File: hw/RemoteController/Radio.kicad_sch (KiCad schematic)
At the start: 49 parts, among them J4 BWSMA-KE-Z001, U10 H3-TCD-12-222X+, U5 XA17-G4K, U8 AD8313xRM, U9 GVA-63, Y2 6.6128 MHz, Y3 10.7 MHz, Y4 13.56 MHz

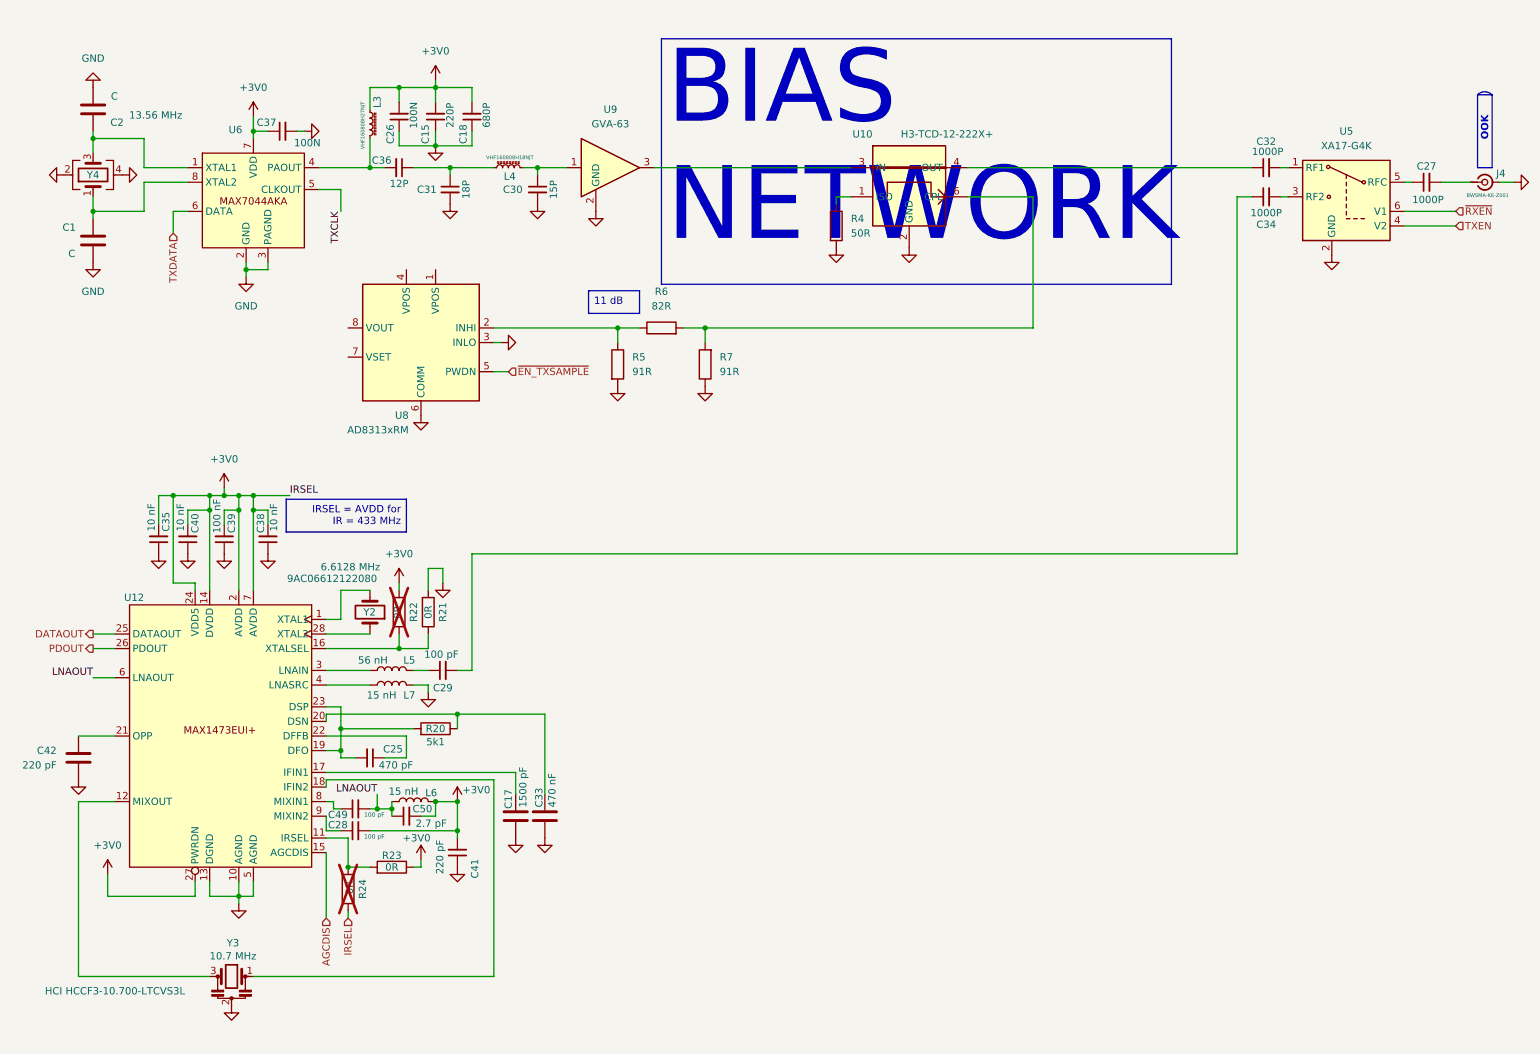
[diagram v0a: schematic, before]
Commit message: remote_ctrl: finish schematic
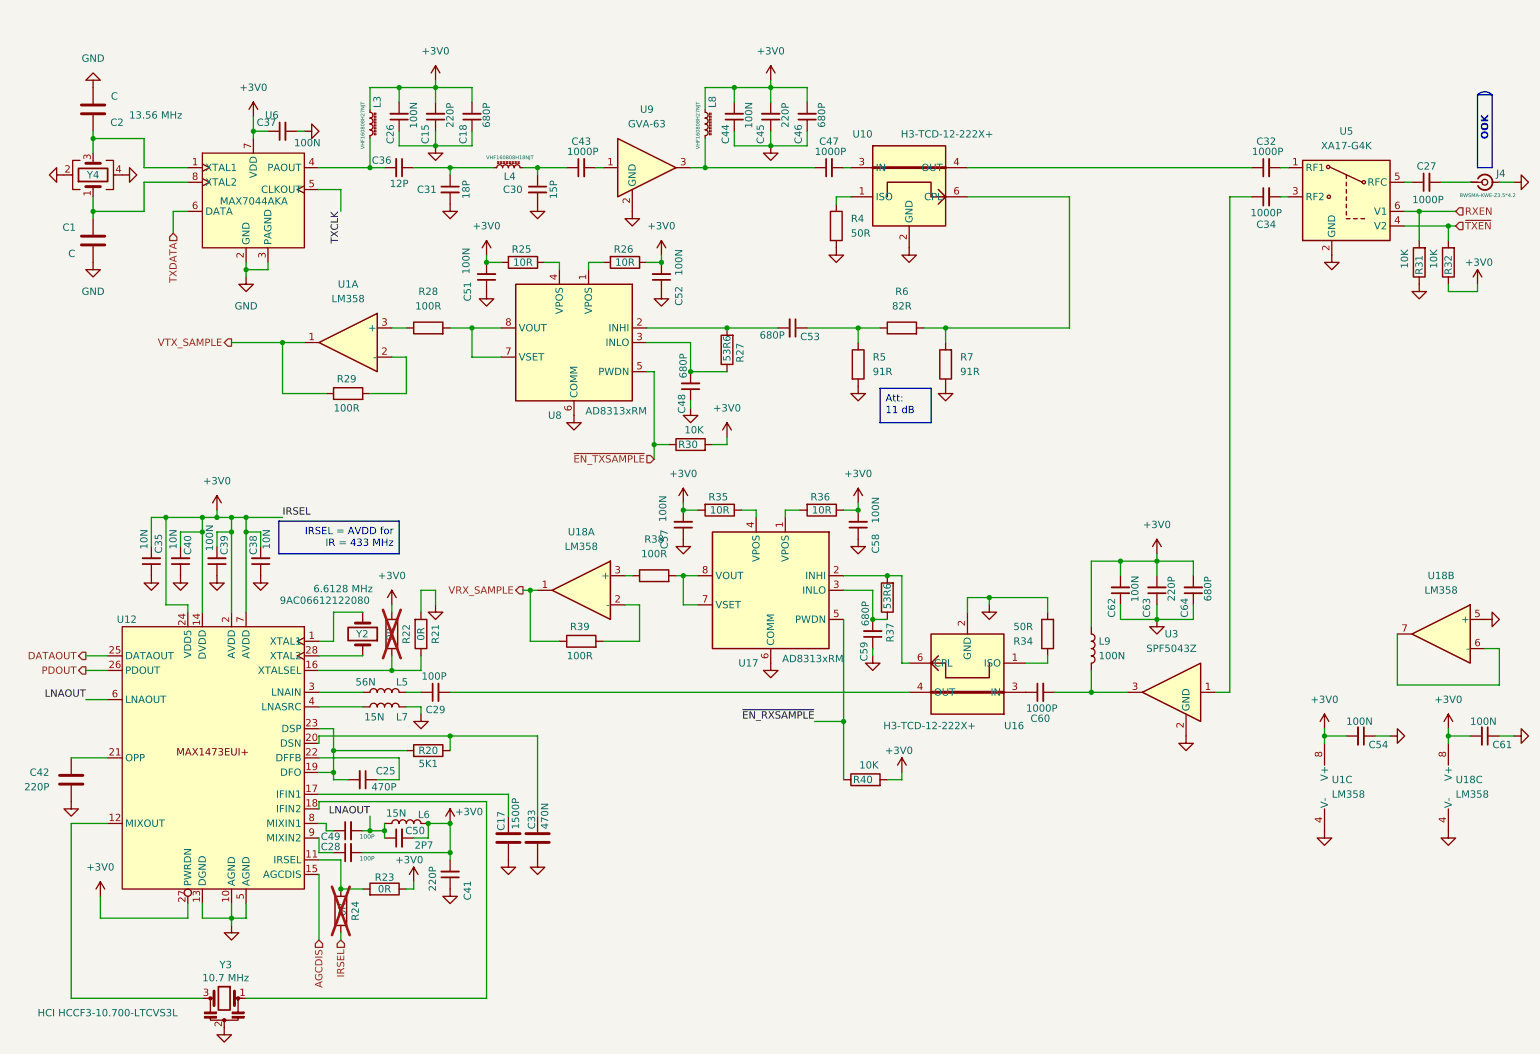
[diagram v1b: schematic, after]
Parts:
- added C43, C47, C60: 1000P, Capacitor_SMD:C_0603_1608Metric_Pad1.08x0.95mm_HandSolder, symbol Device:C_Small
- added C44, C51, C52, C54, C57, C58, C61, C62: 100N, Capacitor_SMD:C_0603_1608Metric_Pad1.08x0.95mm_HandSolder, symbol Device:C_Small
- added C45, C63: 220P, Capacitor_SMD:C_0603_1608Metric_Pad1.08x0.95mm_HandSolder, symbol Device:C_Small
- added C46, C48, C53, C59, C64: 680P, Capacitor_SMD:C_0603_1608Metric_Pad1.08x0.95mm_HandSolder, symbol Device:C_Small
- added L8: 27N, Inductor_SMD:L_0603_1608Metric_Pad1.05x0.95mm_HandSolder, symbol Device:L_Ferrite_Small
- added L9: 100N, Inductor_SMD:L_0603_1608Metric_Pad1.05x0.95mm_HandSolder, symbol Device:L
- added R25, R26, R35, R36: 10R, Resistor_SMD:R_0603_1608Metric_Pad0.98x0.95mm_HandSolder, symbol Device:R
- added R27, R37: 53R6, Resistor_SMD:R_0603_1608Metric_Pad0.98x0.95mm_HandSolder, symbol Device:R
- added R28, R29, R38, R39: 100R, Resistor_SMD:R_0603_1608Metric_Pad0.98x0.95mm_HandSolder, symbol Device:R
- added R30, R31, R32, R40: 10K, Resistor_SMD:R_0603_1608Metric_Pad0.98x0.95mm_HandSolder, symbol Device:R
- added R34: 50R, Resistor_SMD:R_0603_1608Metric_Pad0.98x0.95mm_HandSolder, symbol Device:R
- added U1, U18: LM358, Package_SO:SOIC-8_3.9x4.9mm_P1.27mm, symbol Amplifier_Operational:LM358
- added U16: H3-TCD-12-222X+, symbol steew:H3-TCD-12-222X+
- added U17: AD8313xRM, Package_SO:MSOP-8_3x3mm_P0.65mm, symbol RF_Amplifier:AD8313xRM
- added U3: SPF5043Z, Package_TO_SOT_SMD:SOT-343_SC-70-4, symbol steew:SPF5043Z
- C17: value 1500 pF -> 1500P
- C25: value 470 pF -> 470P
- C28, C29, C49: value 100 pF -> 100P
- C33: value 470 nF -> 470N
- C35, C38, C40: value 10 nF -> 10N
- C39: value 100 nF -> 100N
- C41, C42: value 220 pF -> 220P
- C50: value 2.7 pF -> 2P7
- J4: value BWSMA-KE-Z001 -> BWSMA-KWE-Z3.5*4.2; footprint Connector_Coaxial:SMB_Jack_Vertical -> Connector_Coaxial:SMA_BAT_Wireless_BWSMA-KWE-Z001; PN BWSMA-KE-Z001 -> BWSMA-KWE-Z3.5*4.2
- L5: value 56 nH -> 56N
- L6, L7: value 15 nH -> 15N
- R20: value 5k1 -> 5K1
- U6: value (none) -> MAX7044AKA; footprint steew:MAX7044AKA -> Package_TO_SOT_SMD:TSOT-23-8_HandSoldering
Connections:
- net +3V0: now also C44.2, C45.2, C46.2, C51.2, C52.2, C54.2, C57.2, C58.2, C61.2, C62.2, C63.2, C64.2, L8.1, L9.1, R25.2, R26.1, R30.2, R32.1, R35.2, R36.1, R40.2, U1.8 (V+), U18.8 (V+)
- net GND: now also C44.1, C45.1, C46.1, C48.1, C51.1, C52.1, C54.1, C57.1, C58.1, C59.1, C61.1, C62.1, C63.1, C64.1, R31.1, R34.2, U1.4 (V-), U16.2 (GND), U17.6 (COMM), U18.4 (V-), U18.5 (+), U3.2 (GND), U3.4 (GND); no longer U8.3 (INLO)
- net ~{EN_TXSAMPLE}: now also R30.1
- net at C30.1, L4.2: now also C43.1; no longer U9.1
- net at R5.1, R6.1: now also C53.1; no longer U8.2 (INHI)
- net at U8.1 (VPOS): now also R26.2
- net at U8.4 (VPOS): now also R25.1
- net at U8.7 (VSET): now also U8.8 (VOUT), R28.2
- net at U9.3: now also C47.1, L8.2; no longer U10.3 (IN)
- net at C34.1: now also U3.1; no longer C29.2
- net TXEN renamed ~{TXEN}
- net ~{TXEN}: now also R32.2
- net ~{RXEN} renamed RXEN
- net RXEN: now also R31.2
- new net: C60.2, L9.2, U3.3
- new net: R36.2, U17.1 (VPOS)
- new net: R37.2, U16.6 (CPL), U17.2 (INHI)
- new net: C59.2, R37.1, U17.3 (INLO)
- new net: R35.1, U17.4 (VPOS)
- new net: R38.2, U17.7 (VSET), U17.8 (VOUT)
- new net: R34.1, U16.1 (ISO)
- new net: C47.2, U10.3 (IN)
- new net: C60.1, U16.3 (IN)
- new net: C29.2, U16.4 (OUT)
- new net: C53.2, R27.2, U8.2 (INHI)
- new net: C48.2, R27.1, U8.3 (INLO)
- new net: R28.1, U1.3 (+)
- new net: U18.6 (-), U18.7
- new net: C43.2, U9.1
- new net: R39.2, U18.2 (-)
- new net: R38.1, U18.3 (+)
- new net: R29.2, U1.2 (-)
- new net VRX_SAMPLE: R39.1, U18.1
- new net VTX_SAMPLE: R29.1, U1.1
- new net ~{EN_RXSAMPLE}: R40.1, U17.5 (PWDN)
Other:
- moved on the sheet: C17, C25, C28, C29, C33, C35, C38, C39, C40, C41, C42, C49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

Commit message: remote_ctrl: re-start PCB
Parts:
- U12: value (none) -> MAX1473EUI+; footprint steew:MAX1473EUI+ -> Package_SO:TSSOP-28_4.4x9.7mm_P0.65mm
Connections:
- net at U16.4 (OUT): now also C29.2
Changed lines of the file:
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@@
-	)
-	(symbol
-		(lib_id "steew:MAX1473EUI+")
-		(at 64.77 121.92 0)
-		(mirror y)
-		(unit 1)
-		(body_style 1)
-		(exclude_from_sim no)
-		(in_bom yes)
-		(on_board yes)
-		(in_pos_files yes)
-		(dnp no)
-		(property "Reference" "U12"
-			(at 38.1 121.92 0)
-			(show_name no)
-			(do_not_autoplace no)
-			(effects
-				(font
-					(size 1.27 1.27)
-				)
-				(justify left)
-			)
-		)
-		(property "Value" ""
-			(at 44.8467 121.92 0)
-			(show_name no)
-			(do_not_autoplace no)
-			(effects
-				(font
-					(size 1.27 1.27)
-				)
-				(justify left)
-			)
-		)
-		(property "Footprint" "steew:MAX1473EUI+"
-			(at 64.77 121.92 0)
-			(hide yes)
-			(show_name no)
-			(do_not_autoplace no)
-			(effects
-				(font
-					(size 1.27 1.27)
-				)
-			)
-		)
-		(property "Datasheet" ""
-			(at 64.77 121.92 0)
-			(hide yes)
-			(show_name no)
-			(do_not_autoplace no)
-			(effects
-				(font
-					(size 1.27 1.27)
-				)
-			)
-		)
-		(property "Description" ""
-			(at 64.77 121.92 0)
-			(hide yes)
-			(show_name no)
-			(do_not_autoplace no)
-			(effects
-				(font
-					(size 1.27 1.27)
-				)
-			)
-		)
-		(pin "13"
-		)
-		(pin "25"
-		)
-		(pin "9"
-		)
-		(pin "15"
-		)
-		(pin "21"
-		)
-		(pin "26"
-		)
-		(pin "18"
-		)
-		(pin "19"
-		)
-		(pin "5"
-		)
-		(pin "10"
-		)
-		(pin "20"
-		)
-		(pin "14"
-		)
-		(pin "11"
-		)
-		(pin "12"
-		)
-		(pin "22"
-		)
-		(pin "23"
-		)
-		(pin "4"
-		)
-		(pin "3"
-		)
-		(pin "16"
-		)
-		(pin "28"
-		)
-		(pin "1"
-		)
-		(pin "7"
-		)
-		(pin "17"
-		)
-		(pin "24"
-		)
-		(pin "2"
-		)
-		(pin "8"
-		)
-		(pin "6"
-		)
-		(pin "27"
-		)
-		(instances
-			(project "RemoteController"
-				(path "/2496396e-da71-4b2e-9ac4-452e5130442d/d59aad70-30f5-48a2-8092-bdb11e43ed29"
-					(reference "U12")
-					(unit 1)
-				)
-			)
-		)
 	)
 	(symbol
@@
 					(unit 1)
 				)
+			)
+		)
+	)
+	(symbol
+		(lib_id "steew:MAX1473EUI+")
+		(at 52.07 123.19 0)
+		(unit 1)
+		(body_style 1)
+		(exclude_from_sim no)
+		(in_bom yes)
+		(on_board yes)
+		(in_pos_files yes)
+		(dnp no)
+		(property "Reference" "U12"
+			(at 45.466 143.002 0)
+			(show_name no)
+			(do_not_autoplace no)
+			(effects
+				(font
+					(size 1.27 1.27)
+				)
+				(justify left)
+			)
+		)
+		(property "Value" "MAX1473EUI+"
+			(at 45.466 145.034 0)
+			(show_name no)
+			(do_not_autoplace no)
+			(effects
+				(font
+					(size 1.27 1.27)
+				)
+				(justify left)
+			)
+		)
+		(property "Footprint" "Package_SO:TSSOP-28_4.4x9.7mm_P0.65mm"
+			(at 52.07 123.19 0)
+			(hide yes)
+			(show_name no)
+			(do_not_autoplace no)
+			(effects
+				(font
+					(size 1.27 1.27)
+				)
+			)
+		)
+		(property "Datasheet" "https://www.analog.com/media/en/technical-documentation/data-sheets/MAX1473.pdf"
+			(at 52.07 123.19 0)
+			(hide yes)
+			(show_name no)
+			(do_not_autoplace no)
+			(effects
+				(font
+					(size 1.27 1.27)
+				)
+			)
+		)
+		(property "Description" ""
+			(at 52.07 123.19 0)
+			(hide yes)
+			(show_name no)
+			(do_not_autoplace no)
+			(effects
+				(font
+					(size 1.27 1.27)
+				)
+			)
+		)
+		(pin "13"
+		)
+		(pin "25"
+		)
+		(pin "9"
+		)
+		(pin "15"
+		)
+		(pin "21"
+		)
+		(pin "26"
+		)
+		(pin "18"
+		)
+		(pin "19"
+		)
+		(pin "5"
+		)
+		(pin "10"
+		)
+		(pin "20"
+		)
+		(pin "14"
+		)
+		(pin "11"
+		)
+		(pin "12"
+		)
+		(pin "22"
+		)
+		(pin "23"
+		)
+		(pin "4"
+		)
+		(pin "3"
+		)
+		(pin "16"
+		)
+		(pin "28"
+		)
+		(pin "1"
+		)
+		(pin "7"
+		)
+		(pin "17"
+		)
+		(pin "24"
+		)
+		(pin "2"
+		)
+		(pin "8"
+		)
+		(pin "6"
+		)
+		(pin "27"
+		)
+		(instances
+			(project "RemoteController"
+				(path "/2496396e-da71-4b2e-9ac4-452e5130442d/d59aad70-30f5-48a2-8092-bdb11e43ed29"
+					(reference "U12")
+					(unit 1)
+				)

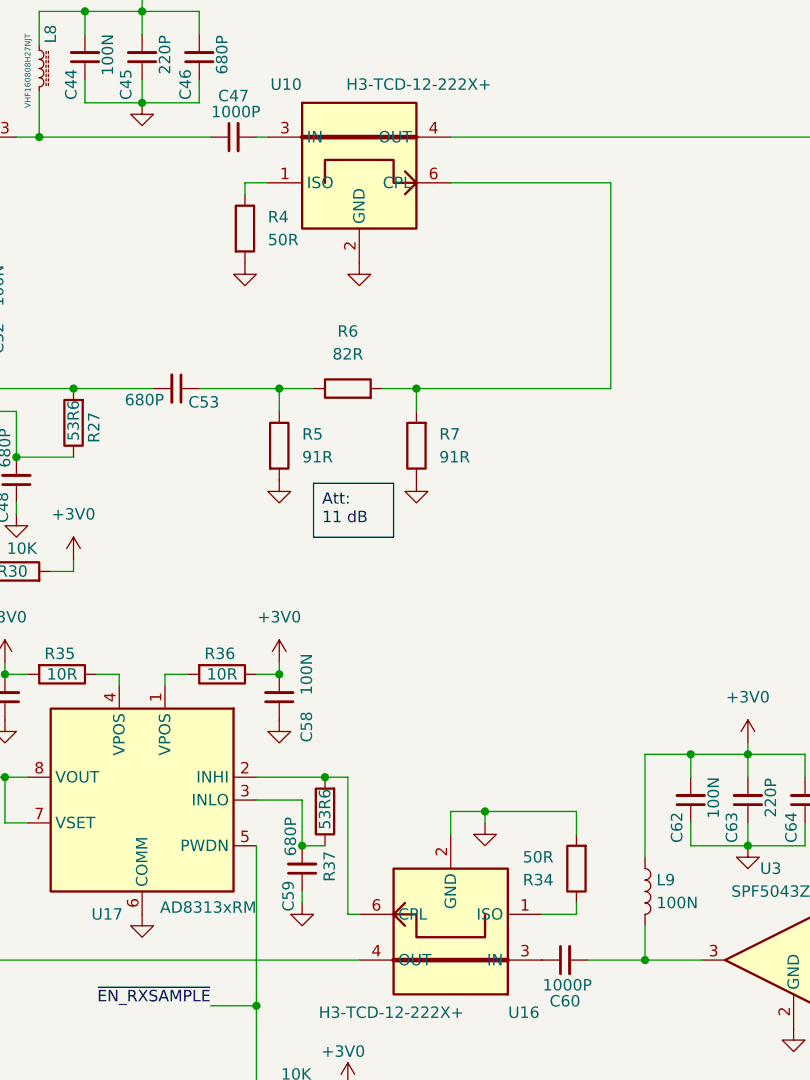
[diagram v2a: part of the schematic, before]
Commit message: remote_ctrl: start laying out RF components
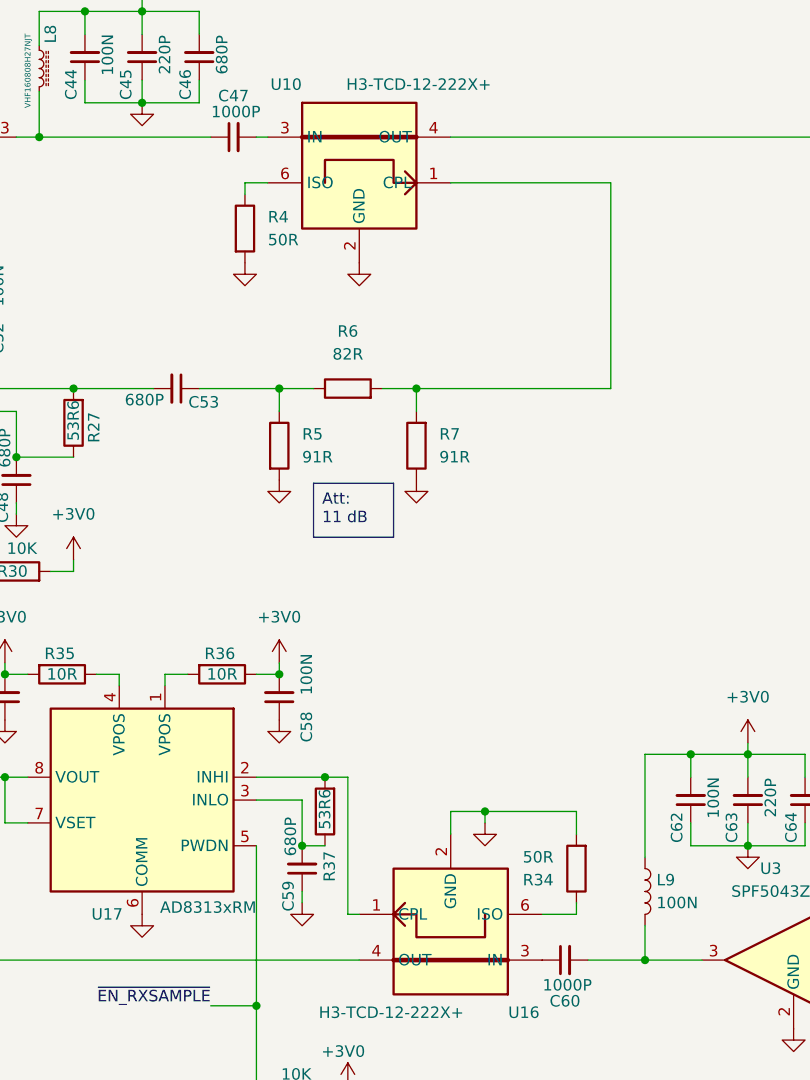
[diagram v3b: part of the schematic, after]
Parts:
- C1, C15, C17, C18, C2, C25, C26, C27, C28, C29, C30, C31, C32, C33, C34, C35, C36, C37, C38, C39, C40, C41, C42, C43, C44, C45, C46, C47, C48, C49, C50, C51, C52, C53, C54, C57, C58, C59, C60, C61, C62, C63, C64: footprint Capacitor_SMD:C_0603_1608Metric_Pad1.08x0.95mm_HandSolder -> Capacitor_SMD:C_0402_1005Metric_Pad0.74x0.62mm_HandSolder
- R20, R21, R22, R23, R24, R25, R26, R27, R28, R29, R30, R31, R32, R34, R35, R36, R37, R38, R39, R4, R40, R5, R6, R7: footprint Resistor_SMD:R_0603_1608Metric_Pad0.98x0.95mm_HandSolder -> Resistor_SMD:R_0402_1005Metric_Pad0.72x0.64mm_HandSolder
- U10, U16: footprint (none) -> RF_Mini-Circuits:Mini-Circuits_DB1627
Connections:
- net at R37.2, U17.2 (INHI): now also U16.1 (CPL); no longer U16.6 (CPL)
- net at R34.1: now also U16.6 (ISO); no longer U16.1 (ISO)
- net at U16.4 (OUT): now also C29.2
- net at R6.2, R7.2: now also U10.1 (CPL); no longer U10.6 (CPL)
- net at R4.1: now also U10.6 (ISO); no longer U10.1 (ISO)

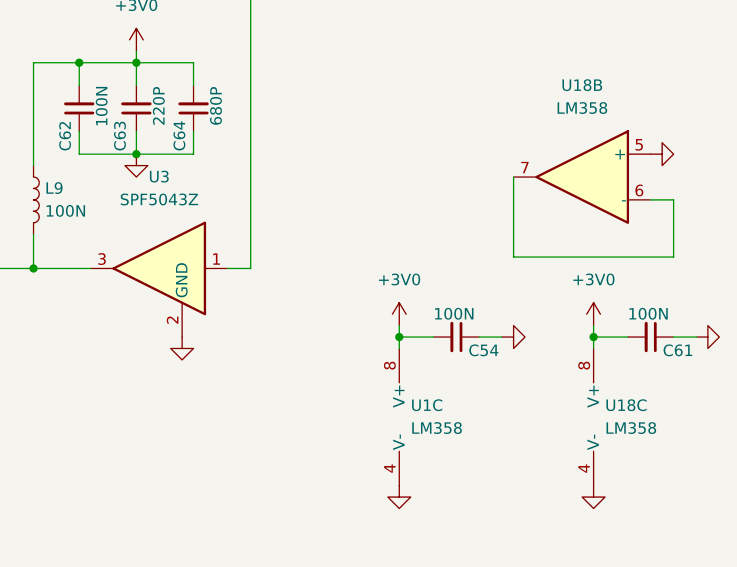
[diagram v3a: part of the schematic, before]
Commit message: remote_ctrl: add RF net class
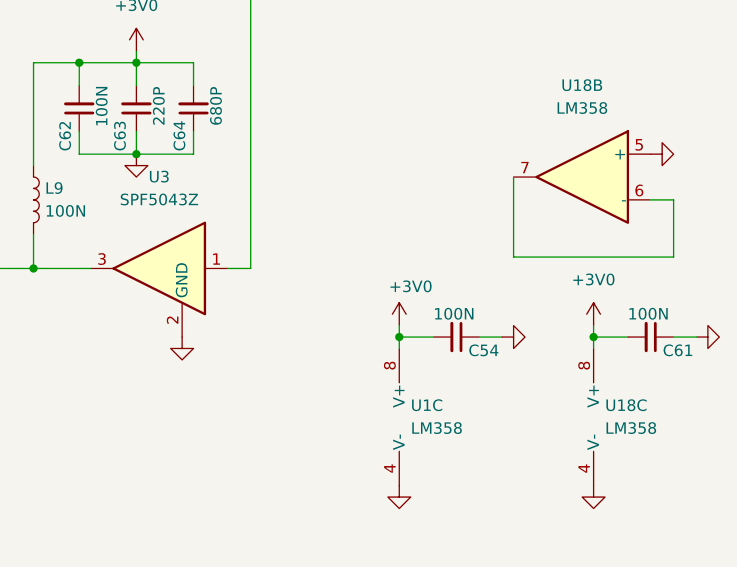
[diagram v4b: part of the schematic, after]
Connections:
- net at U16.4 (OUT): now also C29.2
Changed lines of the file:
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@@
 		)
 	)
+	(rule_area
+		(exclude_from_sim no)
+		(in_bom yes)
+		(on_board yes)
+		(dnp no)
+		(polyline
+			(pts
+				(xy 71.12 19.05) (xy 71.12 52.07) (xy 135.89 52.07) (xy 135.89 72.39) (xy 130.81 77.47) (xy 130.81 87.63)
+				(xy 160.02 87.63) (xy 172.72 100.33) (xy 172.72 105.41) (xy 166.37 111.76) (xy 161.29 111.76) (xy 160.02 113.03)
+				(xy 160.02 129.54) (xy 158.115 132.08) (xy 121.285 132.08) (xy 113.03 132.08) (xy 113.03 142.24)
+				(xy 113.03 151.13) (xy 113.03 157.48) (xy 114.3 157.48) (xy 119.38 157.48) (xy 123.825 157.48) (xy 143.51 157.48)
+				(xy 184.15 157.48) (xy 220.98 157.48) (xy 248.92 129.54) (xy 248.92 80.01) (xy 252.73 76.2) (xy 269.24 76.2)
+				(xy 281.94 63.5) (xy 281.94 26.67) (xy 274.32 19.05)
+			)
+			(stroke
+				(width 0)
+				(type dash)
+			)
+			(fill
+				(type none)
+			)
+		)
+	)
+	(netclass_flag ""
+		(length 2.54)
+		(shape round)
+		(at 106.68 19.05 0)
+		(fields_autoplaced yes)
+		(effects
+			(font
+				(size 1.27 1.27)
+			)
+			(justify left bottom)
+		)
+		(property "Net Class" "RF"
+			(at 107.3785 16.51 0)
+			(show_name no)
+			(do_not_autoplace no)
+			(effects
+				(font
+					(size 1.27 1.27)
+				)
+				(justify left)
+			)
+		)
+		(property "Component Class" ""
+			(at 54.61 15.24 0)
+			(show_name no)
+			(do_not_autoplace no)
+			(effects
+				(font
+					(size 1.27 1.27)
+					(italic yes)
+				)
+			)
+		)
+	)
 	(symbol
 		(lib_id "Device:R")
@@
 		(in_pos_files yes)
 		(dnp no)
-		(fields_autoplaced yes)
 		(property "Reference" "#PWR016"
 			(at 245.11 144.78 0)
@@
 		)
 		(property "Value" "+3V0"
-			(at 245.11 135.89 0)
+			(at 246.38 136.652 0)
 			(show_name no)
 			(do_not_autoplace no)
